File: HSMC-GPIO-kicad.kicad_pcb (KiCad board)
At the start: 2 copper layers, 63.5 x 78.1 mm, 111 parts, among them J1 HSMC, J2 Conn_01x03_Male, J3 I2C, J4 Screw_Terminal_01x04, J5 Conn_02x20_Odd_Even, U1 MC78M05_TO252, U2 PCA9507

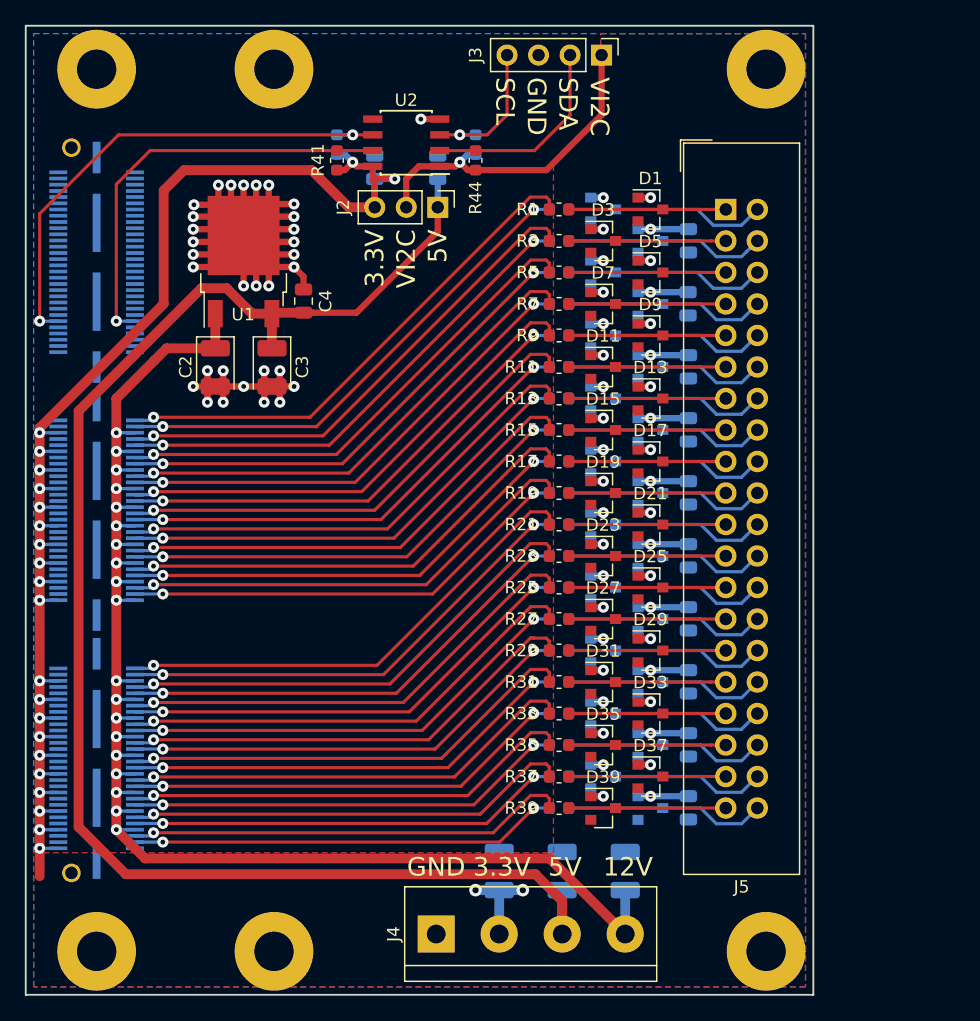
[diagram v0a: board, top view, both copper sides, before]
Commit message: Modify and submit to Sunstone for DFM report.
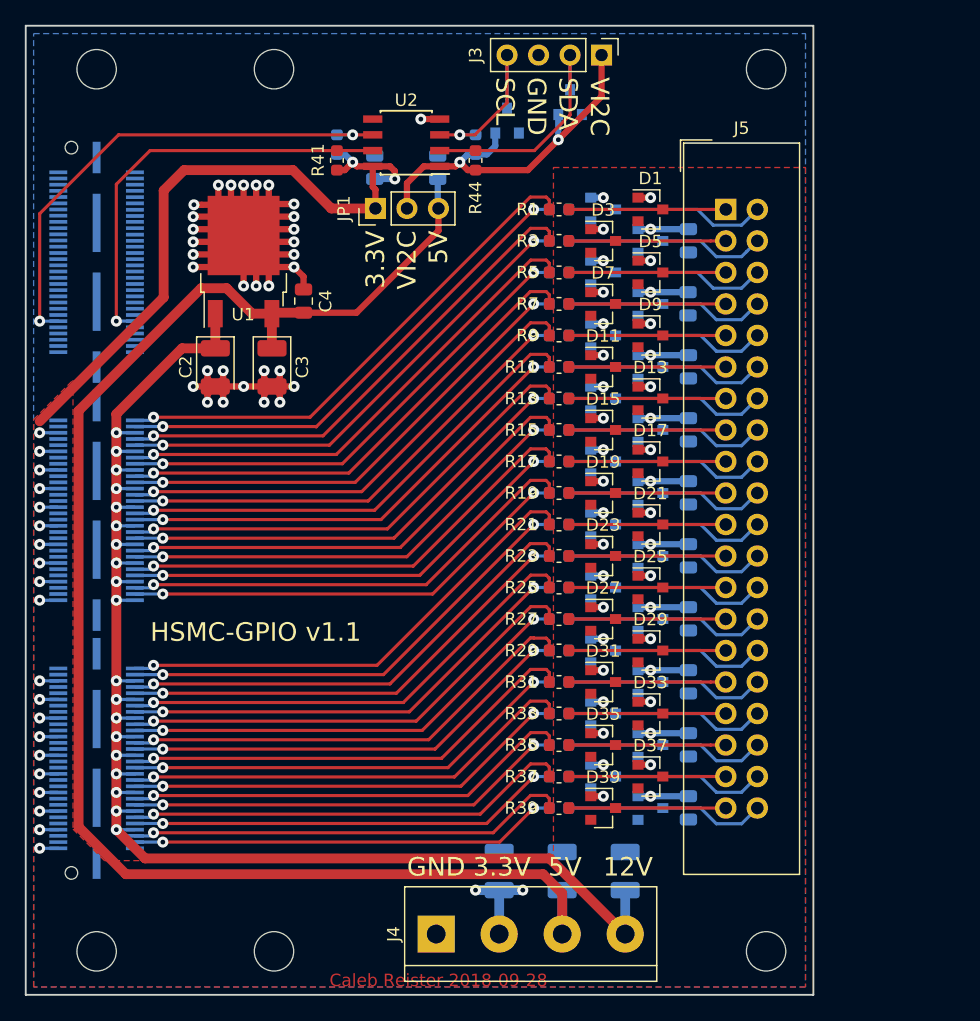
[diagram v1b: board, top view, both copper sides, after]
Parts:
- added D41: BAT54S, Package_TO_SOT_SMD:SOT-23, B.Cu at (69.3, 31.6)
- added D42: BAT54S, Package_TO_SOT_SMD:SOT-23, B.Cu at (64.2, 33.1)
- J1: value HSMC -> HSMC_Card_QTH; footprint HSMC:HSMC_Card_QTH-090-01-L-D-A -> Connector_Samtec:Samtec_HSMC_Card_QTH-090-01-x-D-A_3.076x0.932in_P0.5mm_Vertical
- JP1: renamed from J2; value Conn_01x03_Male -> Jumper_3_Bridged12
- moved JP1 5.02 mm to (53.6, 40.1), turned to 90 degrees
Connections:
- J1 pad 100: +12V -> /GPIO13
- J1 pad 101: Net-(J1-Pad101) -> +3V3
- J1 pad 102: /GPIO20 -> +12V
- J1 pad 104: /GPIO21 -> /GPIO14
- J1 pad 105: +3V3 -> Net-(J1-Pad105)
- J1 pad 106: +12V -> /GPIO15
- J1 pad 107: Net-(J1-Pad107) -> +3V3
- J1 pad 108: /GPIO22 -> +12V
- J1 pad 11: Net-(J1-Pad11) -> GND
- J1 pad 110: /GPIO23 -> /GPIO16
- J1 pad 111: +3V3 -> Net-(J1-Pad111)
- J1 pad 112: +12V -> /GPIO17
- J1 pad 113: Net-(J1-Pad113) -> +3V3
- J1 pad 114: /GPIO24 -> +12V
- J1 pad 116: /GPIO25 -> /GPIO18
- J1 pad 117: +3V3 -> Net-(J1-Pad117)
- J1 pad 118: +12V -> /GPIO19
- J1 pad 119: Net-(J1-Pad119) -> +3V3
- J1 pad 12: Net-(J1-Pad12) -> GND
- J1 pad 120: /GPIO26 -> +12V
- J1 pad 122: /GPIO27 -> /GPIO20
- J1 pad 123: +3V3 -> Net-(J1-Pad123)
- J1 pad 124: +12V -> /GPIO21
- J1 pad 125: Net-(J1-Pad125) -> +3V3
- J1 pad 126: /GPIO28 -> +12V
- J1 pad 128: /GPIO29 -> /GPIO22
- J1 pad 129: +3V3 -> Net-(J1-Pad129)
- J1 pad 130: +12V -> /GPIO23
- J1 pad 131: Net-(J1-Pad131) -> +3V3
- J1 pad 132: /GPIO30 -> +12V
- J1 pad 134: /GPIO31 -> /GPIO24
- J1 pad 135: +3V3 -> Net-(J1-Pad135)
- J1 pad 136: +12V -> /GPIO25
- J1 pad 137: Net-(J1-Pad137) -> +3V3
- J1 pad 138: /GPIO32 -> +12V
- J1 pad 140: /GPIO33 -> /GPIO26
- J1 pad 141: +3V3 -> Net-(J1-Pad141)
- J1 pad 142: +12V -> /GPIO27
- J1 pad 143: Net-(J1-Pad143) -> +3V3
- J1 pad 144: /GPIO34 -> +12V
- J1 pad 146: /GPIO35 -> /GPIO28
- J1 pad 147: +3V3 -> Net-(J1-Pad147)
- J1 pad 148: +12V -> /GPIO29
- J1 pad 149: Net-(J1-Pad149) -> +3V3
- J1 pad 150: /GPIO36 -> +12V
- J1 pad 152: /GPIO37 -> /GPIO30
- J1 pad 153: +3V3 -> Net-(J1-Pad153)
- J1 pad 154: +12V -> /GPIO31
- J1 pad 155: Net-(J1-Pad155) -> +3V3
- J1 pad 156: /GPIO38 -> +12V
- J1 pad 158: /GPIO39 -> /GPIO32
- J1 pad 159: +3V3 -> Net-(J1-Pad159)
- J1 pad 160: GND -> /GPIO33
- J1 pad 161: GND -> +3V3
- J1 pad 162: GND -> +12V
- J1 pad 163: GND -> Net-(J1-Pad163)
- J1 pad 164: GND -> /GPIO34
- J1 pad 165: GND -> Net-(J1-Pad165)
- J1 pad 166: GND -> /GPIO35
- J1 pad 167: GND -> +3V3
- J1 pad 168: GND -> +12V
- J1 pad 169: GND -> Net-(J1-Pad169)
- J1 pad 17: Net-(J1-Pad17) -> GND
- J1 pad 170: GND -> /GPIO36
- J1 pad 171: GND -> Net-(J1-Pad171)
- J1 pad 172: GND -> /GPIO37
- J1 pad 18: Net-(J1-Pad18) -> GND
- J1 pad 23: Net-(J1-Pad23) -> GND
- J1 pad 24: Net-(J1-Pad24) -> GND
- J1 pad 29: Net-(J1-Pad29) -> GND
- J1 pad 30: Net-(J1-Pad30) -> GND
- J1 pad 33: /SDA -> Net-(J1-Pad33)
- J1 pad 34: /SCL -> Net-(J1-Pad34)
- J1 pad 35: Net-(J1-Pad35) -> GND
- J1 pad 36: Net-(J1-Pad36) -> GND
- J1 pad 41: Net-(J1-Pad41) -> GND
- J1 pad 42: /GPIO0 -> GND
- J1 pad 44: /GPIO1 -> Net-(J1-Pad44)
- J1 pad 45: +3V3 -> Net-(J1-Pad45)
- J1 pad 46: +12V -> Net-(J1-Pad46)
- J1 pad 47: Net-(J1-Pad47) -> GND
- J1 pad 48: /GPIO2 -> GND
- J1 pad 49: Net-(J1-Pad49) -> /SDA
- J1 pad 5: Net-(J1-Pad5) -> GND
- J1 pad 50: /GPIO3 -> /SCL
- J1 pad 51: +3V3 -> Net-(J1-Pad51)
- J1 pad 52: +12V -> Net-(J1-Pad52)
- J1 pad 53: Net-(J1-Pad53) -> GND
- J1 pad 54: /GPIO4 -> GND
- J1 pad 56: /GPIO5 -> Net-(J1-Pad56)
- J1 pad 57: +3V3 -> Net-(J1-Pad57)
- J1 pad 58: +12V -> Net-(J1-Pad58)
- J1 pad 59: Net-(J1-Pad59) -> GND
- J1 pad 6: Net-(J1-Pad6) -> GND
- J1 pad 60: /GPIO6 -> GND
- J1 pad 62: /GPIO7 -> /GPIO0
- J1 pad 63: +3V3 -> Net-(J1-Pad63)
- J1 pad 64: +12V -> /GPIO1
- J1 pad 65: Net-(J1-Pad65) -> +3V3
- J1 pad 66: /GPIO8 -> +12V
- J1 pad 68: /GPIO9 -> /GPIO2
- J1 pad 69: +3V3 -> Net-(J1-Pad69)
- J1 pad 70: +12V -> /GPIO3
- J1 pad 71: Net-(J1-Pad71) -> +3V3
- J1 pad 72: /GPIO10 -> +12V
- J1 pad 74: /GPIO11 -> /GPIO4
- J1 pad 75: +3V3 -> Net-(J1-Pad75)
- J1 pad 76: +12V -> /GPIO5
- J1 pad 77: Net-(J1-Pad77) -> +3V3
- J1 pad 78: /GPIO12 -> +12V
- J1 pad 80: /GPIO13 -> /GPIO6
- J1 pad 81: +3V3 -> Net-(J1-Pad81)
- J1 pad 82: +12V -> /GPIO7
- J1 pad 83: Net-(J1-Pad83) -> +3V3
- J1 pad 84: /GPIO14 -> +12V
- J1 pad 86: /GPIO15 -> /GPIO8
- J1 pad 87: +3V3 -> Net-(J1-Pad87)
- J1 pad 88: +12V -> /GPIO9
- J1 pad 89: Net-(J1-Pad89) -> +3V3
- J1 pad 90: /GPIO16 -> +12V
- J1 pad 92: /GPIO17 -> /GPIO10
- J1 pad 93: +3V3 -> Net-(J1-Pad93)
- J1 pad 94: +12V -> /GPIO11
- J1 pad 95: Net-(J1-Pad95) -> +3V3
- J1 pad 96: /GPIO18 -> +12V
- J1 pad 98: /GPIO19 -> /GPIO12
- J1 pad 99: +3V3 -> Net-(J1-Pad99)
- JP1 pad 1: +5V -> +3V3
- JP1 pad 3: +3V3 -> +5V
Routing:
- net +3V3: track 183.0 -> 145.0 mm
- net Net-(D42-Pad3): track 12.2 -> 16.2 mm
- net VBUS: track 27.1 -> 31.0 mm, vias 1 -> 2
- net Net-(D41-Pad3): track 16.5 -> 19.3 mm
- net +12V: track 123.8 -> 123.0 mm
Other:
- board text added: "Caleb Reister 2018-09-28"
- board text added: "HSMC-GPIO v1.1"

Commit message: Re-place protection diodes/resistors, change diode packages to SOT-323
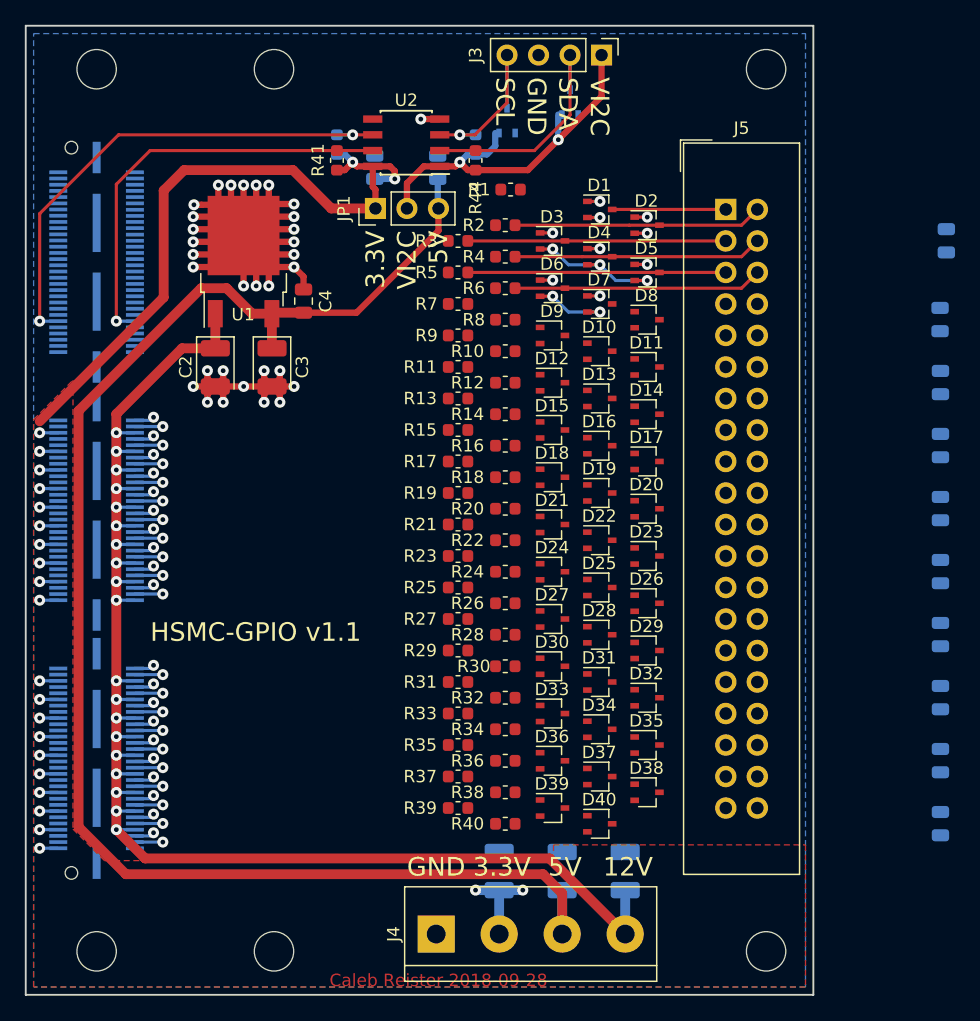
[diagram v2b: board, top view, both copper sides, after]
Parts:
- D1, D11, D13, D15, D17, D19, D21, D23, D25, D27, D29, D3, D31, D33, D35, D37, D39, D41, D42, D5, D7, D9: footprint Package_TO_SOT_SMD:SOT-23 -> Package_TO_SOT_SMD:SOT-323_SC-70
- D10, D12, D14, D16, D18, D2, D20, D22, D24, D26, D28, D30, D32, D34, D36, D38, D4, D40, D6, D8: footprint Package_TO_SOT_SMD:SOT-23 -> Package_TO_SOT_SMD:SOT-323_SC-70; moved to F.Cu
- R10, R12, R14, R16, R18, R2, R20, R22, R24, R26, R28, R30, R32, R34, R36, R38, R4, R40, R6, R8: moved to F.Cu
- moved C16 20.8 mm to (99.6, 42.7)
- moved C10 20.4 mm to (99.1, 74.5)
- moved C11 20.4 mm to (99.1, 69.4)
- moved C12 20.4 mm to (99.1, 64.3)
- moved C13 20.4 mm to (99.1, 59.2)
- moved C14 20.4 mm to (99.1, 54.2)
- moved C15 20.4 mm to (99.1, 49.1)
- moved C7 20.4 mm to (99.1, 89.7)
- moved C8 20.4 mm to (99.1, 84.6)
- moved C9 20.4 mm to (99.1, 79.6)
- moved R11 8.14 mm to (60.3, 52.9)
- moved R13 8.14 mm to (60.3, 55.5)
- moved R15 8.14 mm to (60.3, 58.0)
- moved R17 8.14 mm to (60.3, 60.5)
- moved R19 8.14 mm to (60.3, 63.1)
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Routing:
- net /GPIO0: track 41.7 -> 1.60 mm
- net /GPIO2: track 41.3 -> 1.60 mm
- net /GPIO4: track 40.9 -> 1.60 mm
- net /GPIO6: track 40.4 -> 1.60 mm
- net /GPIO1: track 40.7 -> 2.25 mm, vias 2 -> 1
- net /GPIO8: track 40.0 -> 1.60 mm
- net /GPIO10: track 39.6 -> 1.60 mm
- net /GPIO3: track 40.2 -> 2.25 mm, vias 2 -> 1
- net /GPIO20: track 39.5 -> 1.60 mm
- net /GPIO5: track 39.8 -> 2.25 mm, vias 2 -> 1
- net /GPIO12: track 39.1 -> 1.60 mm
- net /GPIO22: track 39.0 -> 1.60 mm
- net /GPIO14: track 38.7 -> 1.60 mm
- net /GPIO7: track 39.4 -> 2.25 mm, vias 2 -> 1
- net /GPIO24: track 38.6 -> 1.60 mm
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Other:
- net class Power: trace_width 0.508 -> 0.254

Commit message: Reroute GPIO, 5V regulator, and I2C buffer
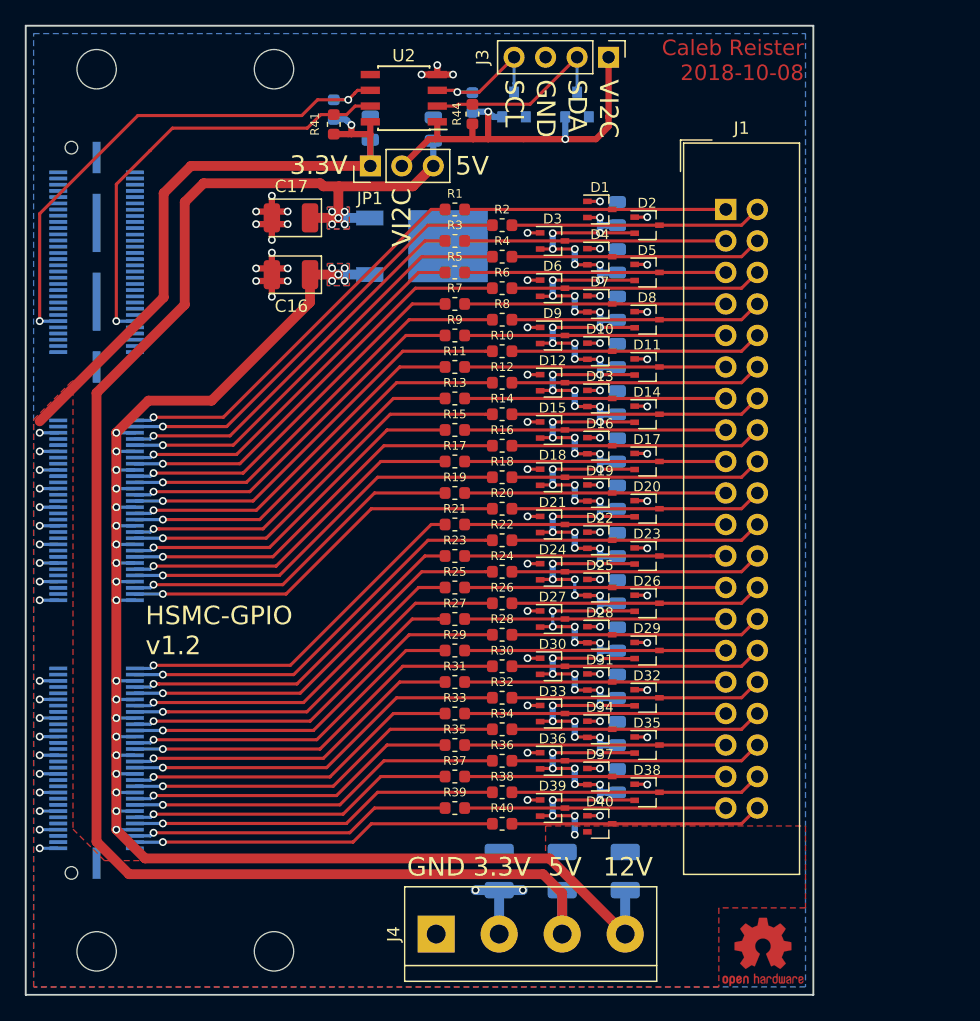
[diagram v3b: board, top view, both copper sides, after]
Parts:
- removed the C4 at (47.8, 47.6)
- removed the C8 at (99.1, 84.6)
- removed MH1, MH2: MountingHole, HSMC:MountingHole
- added C11: 100n, Capacitor_SMD:C_0805_2012Metric, B.Cu at (73.1, 86.3)
- added C12: 100n, Capacitor_SMD:C_0805_2012Metric, B.Cu at (73.1, 82.5)
- added C13: 100n, Capacitor_SMD:C_0805_2012Metric, B.Cu at (73.1, 78.7)
- added C2: 100n, Capacitor_SMD:C_0805_2012Metric, B.Cu at (73.1, 71.0)
- added LOGO1: Logo_Open_Hardware_Small, Symbol:OSHW-Logo2_7.3x6mm_Copper, F.Cu at (84.8, 100.1)
- D41, D42: footprint Package_TO_SOT_SMD:SOT-323_SC-70 -> Package_TO_SOT_SMD:SOT-23
- U1: moved to B.Cu
- moved C1 30.0 mm to (73.1, 74.8), turned to 90 degrees
- moved C3 28.8 mm to (73.1, 67.2), turned to 90 degrees
- moved C4 28.3 mm to (73.1, 63.4), turned to 90 degrees
- moved C5 27.8 mm to (73.1, 59.6), turned to 90 degrees
- moved C6 27.4 mm to (73.1, 55.8), turned to 90 degrees
- moved C7 27.0 mm to (73.1, 52.0), turned to 90 degrees
- moved C8 26.7 mm to (73.1, 48.2), turned to 90 degrees
- moved C10 26.6 mm to (73.1, 40.6), turned to 90 degrees
- moved C9 26.4 mm to (73.1, 44.4), turned to 90 degrees
- moved U1 14.4 mm to (57.3, 43.2), turned to 0 degrees
- moved C17 12.2 mm to (46.8, 40.9), turned to 180 degrees
- moved C16 9.65 mm to (46.8, 45.5), turned to 180 degrees
- moved R1 4.77 mm to (60.0, 40.2)
- moved R44 3.74 mm to (61.4, 32.5)
- moved U2 3.59 mm to (55.9, 31.2)
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- renumbered C7 to C1, C16 to C10, C5 to C14, C6 to C15, C2 to C16, C3 to C17, C20 to C18, C18 to C19, C19 to C20, C9 to C3, C10 to C4, C11 to C5, C12 to C6, C13 to C7, C14 to C8, C15 to C9, J5 to J1, J1 to J2
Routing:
- net +3V3: track 111.8 -> 303.5 mm, vias 31 -> 101
- net GND: track 128.1 -> 63.0 mm, vias 39 -> 55
- net /GPIO1: track 2.25 -> 35.5 mm
- net /GPIO3: track 2.25 -> 35.1 mm
- net /GPIO5: track 2.25 -> 34.7 mm
- net /GPIO7: track 2.25 -> 34.2 mm
- net /GPIO9: track 2.25 -> 33.8 mm
- net /GPIO11: track 2.25 -> 33.4 mm
- net /GPIO21: track 2.25 -> 33.3 mm
- net /GPIO13: track 2.25 -> 33.0 mm
- net /GPIO23: track 2.25 -> 32.9 mm
- net /GPIO0: track 1.60 -> 32.1 mm
- net /GPIO15: track 2.25 -> 32.5 mm
- net /GPIO25: track 2.25 -> 32.4 mm
- net /GPIO2: track 1.60 -> 31.6 mm
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- added copper zone on B.Cu, net +12V
- added copper zone on F.Cu, net +12V
- added copper zone on B.Cu, net +5V
- added copper zone on F.Cu, net +5V
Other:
- net class Default: via_dia 0.889 -> 0.635
- net class Power: trace_width 0.254 -> 0.508; via_dia 0.889 -> 0.635
- rule via_min_size: 0.381 -> 0.254
- board text added: "Caleb Reister 2018-10-08"
- board text added: "HSMC-GPIO v1.2"
- board text removed: "Caleb Reister 2018-09-28"
- board text removed: "HSMC-GPIO v1.1"

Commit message: Minor footprint and position adjustments
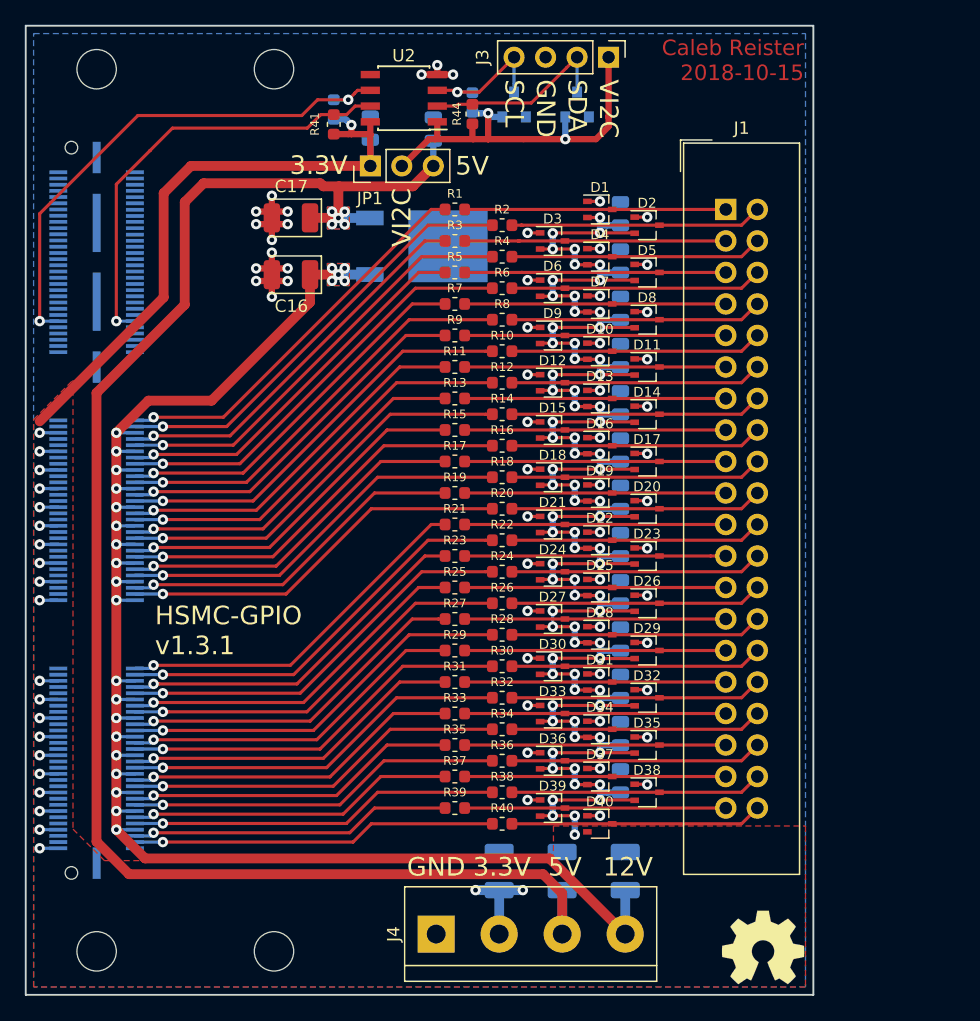
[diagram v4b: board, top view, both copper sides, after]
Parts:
- LOGO1: footprint Symbol:OSHW-Logo2_7.3x6mm_Copper -> Symbol:OSHW-Symbol_6.7x6mm_SilkScreen
- moved C13 38.1 mm to (73.3, 40.6)
- moved C11 38.1 mm to (73.3, 48.2)
- moved C12 38.1 mm to (73.3, 44.4)
- moved C3 11.4 mm to (73.3, 78.7)
- moved C7 11.4 mm to (73.3, 63.4)
- moved C10 11.4 mm to (73.3, 52.0)
- moved C4 11.4 mm to (73.3, 74.8)
- moved C5 11.4 mm to (73.3, 71.0)
- moved C6 11.4 mm to (73.3, 67.2)
- moved C8 11.4 mm to (73.3, 59.6)
- moved C9 11.4 mm to (73.3, 55.8)
- moved C1 11.4 mm to (73.3, 86.3)
- moved C2 11.4 mm to (73.3, 82.5)
- moved LOGO1 0.36 mm to (84.8, 99.7)
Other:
- net class Default: via_dia 0.635 -> 0.8382
- net class Power: via_dia 0.635 -> 0.8382
- rule via_min_size: 0.254 -> 0.381
- board text added: "Caleb Reister 2018-10-15"
- board text added: "HSMC-GPIO v1.3.1"
- board text removed: "Caleb Reister 2018-10-08"
- board text removed: "HSMC-GPIO v1.2"
